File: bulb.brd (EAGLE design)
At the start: 24 x 40 mm, 9 parts, among them U1 RFD22102, U2 IC REG LDO 3.3V

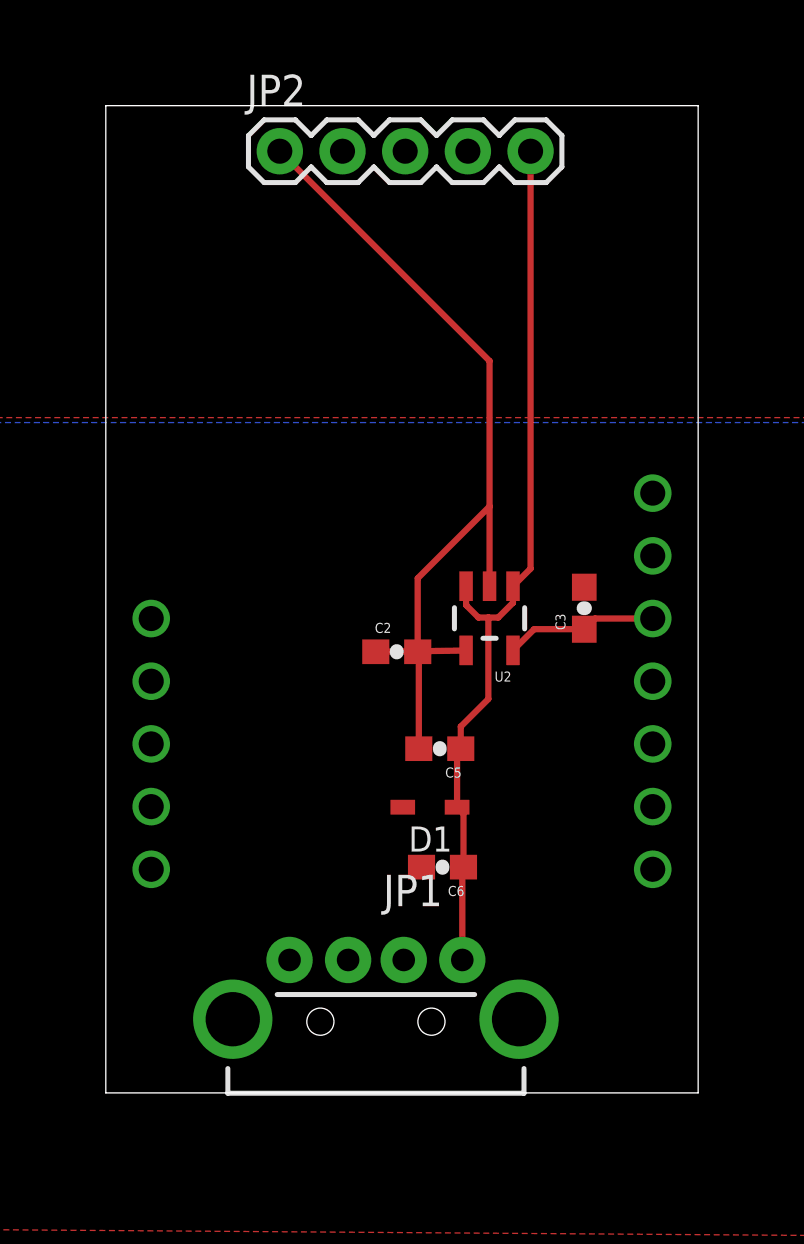
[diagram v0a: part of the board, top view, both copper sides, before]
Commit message: circle pcb, and updated usb pcb
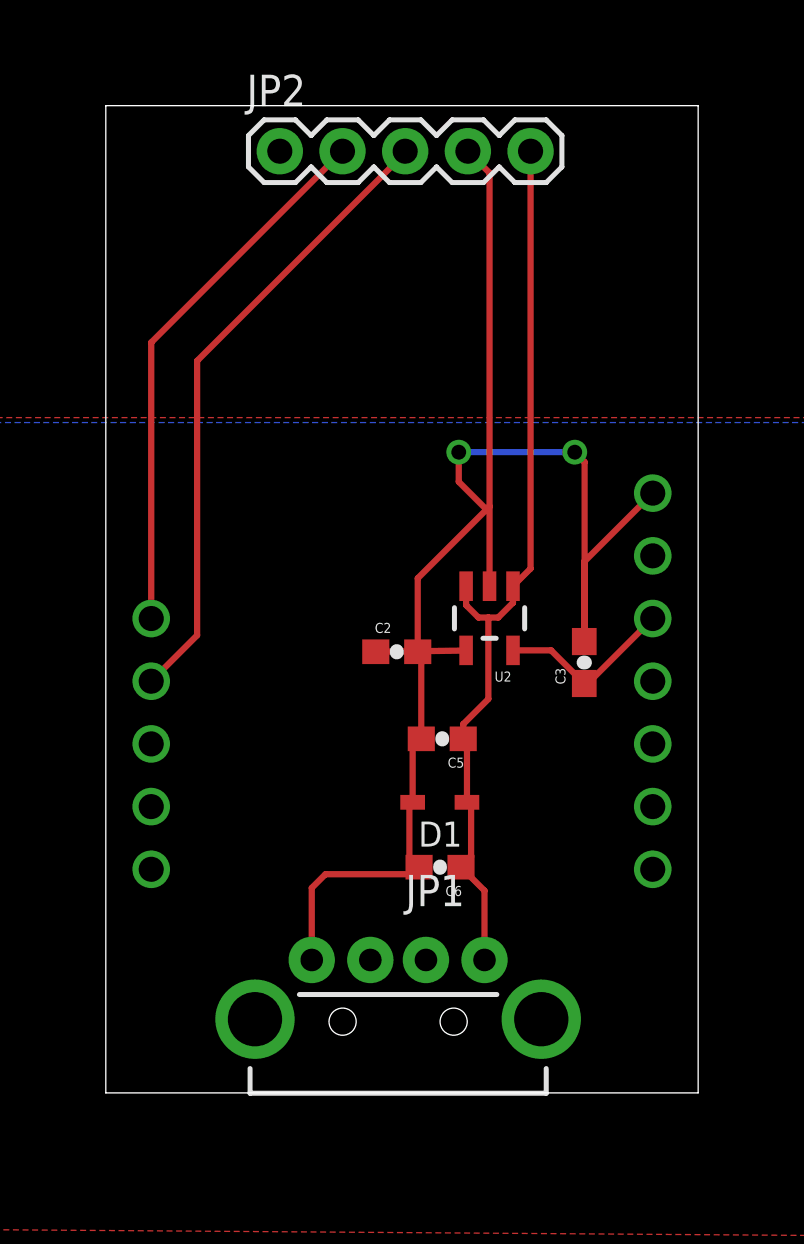
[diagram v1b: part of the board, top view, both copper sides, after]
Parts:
- moved C3 2.20 mm to (20.7, 32.0)
- moved JP1 0.90 mm to (13.1, 17.5)
- moved D1 0.45 mm to (14.8, 26.3)
- moved C5 0.41 mm to (14.9, 28.9)
- moved C6 0.10 mm to (14.8, 23.7)
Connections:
- removed net B: JP2.2
- removed net G: JP2.3
- removed net R: JP2.4
- new net DIN: JP2.3, U1.GPIO5
- new net DOUT: JP2.2, U1.GPIO6
- net GND: now also JP2.4; no longer JP2.1
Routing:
- net GND: track 32.2 -> 64.4 mm, vias 0 -> 2
- net DIN: track 0.00 -> 25.7 mm
- net DOUT: track 0.00 -> 22.1 mm
- net 3.3V: track 6.20 -> 7.31 mm
- net VBUS: track 36.2 -> 36.9 mm
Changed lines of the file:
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@@
 <attribute name="PROD_ID" value="CAP-07884" x="52.458" y="-14.576" size="1.778" layer="27" display="off"/>
 </element>
-<element name="C3" library="SparkFun-Capacitors" package="0603-CAP" value="2.2uF" x="20.686" y="34.178" rot="R90">
-<attribute name="PROD_ID" value="CAP-07888" x="67.676" y="77.358" size="1.778" layer="27" rot="R90" display="off"/>
+<element name="C3" library="SparkFun-Capacitors" package="0603-CAP" value="2.2uF" x="20.686" y="31.978" rot="R90">
+<attribute name="PROD_ID" value="CAP-07888" x="67.676" y="75.158" size="1.778" layer="27" rot="R90" display="off"/>
 </element>
-<element name="C5" library="SparkFun-Capacitors" package="0603-CAP" value="4.7uF" x="14.832" y="28.486" rot="R180">
-<attribute name="PROD_ID" value="CAP-08280" x="-32.158" y="75.476" size="1.778" layer="27" rot="R180" display="off"/>
+<element name="C5" library="SparkFun-Capacitors" package="0603-CAP" value="4.7uF" x="14.932" y="28.886" rot="R180">
+<attribute name="PROD_ID" value="CAP-08280" x="-32.058" y="75.876" size="1.778" layer="27" rot="R180" display="off"/>
 </element>
-<element name="C6" library="SparkFun-Capacitors" package="0603-CAP" value="10nF" x="14.942" y="23.686" rot="R180">
-<attribute name="PROD_ID" value="CAP-00867" x="-35.858" y="70.676" size="1.778" layer="27" rot="R180" display="off"/>
+<element name="C6" library="SparkFun-Capacitors" package="0603-CAP" value="10nF" x="14.842" y="23.686" rot="R180">
+<attribute name="PROD_ID" value="CAP-00867" x="-35.958" y="70.676" size="1.778" layer="27" rot="R180" display="off"/>
 </element>
-<element name="D1" library="zetex" package="SOD323" value="TVS Diode 5VWM 9.8VDC SOD323" x="14.432" y="26.114" rot="R180">
-<attribute name="OC_NEWARK" value="79R6078" x="-21.128" y="73.104" size="1.778" layer="27" rot="R180" display="off"/>
-<attribute name="MPN" value="CDSOD323-T05C" x="-21.128" y="73.104" size="1.778" layer="27" rot="R180" display="off"/>
-<attribute name="MF" value="" x="-21.128" y="73.104" size="1.778" layer="27" rot="R180" display="off"/>
-<attribute name="OC_FARNELL" value="1824860" x="-21.128" y="73.104" size="1.778" layer="27" rot="R180" display="off"/>
+<element name="D1" library="zetex" package="SOD323" value="TVS Diode 5VWM 9.8VDC SOD323" x="14.832" y="26.314" rot="R180">
+<attribute name="OC_NEWARK" value="79R6078" x="-20.728" y="73.304" size="1.778" layer="27" rot="R180" display="off"/>
+<attribute name="MPN" value="CDSOD323-T05C" x="-20.728" y="73.304" size="1.778" layer="27" rot="R180" display="off"/>
+<attribute name="MF" value="" x="-20.728" y="73.304" size="1.778" layer="27" rot="R180" display="off"/>
+<attribute name="OC_FARNELL" value="1824860" x="-20.728" y="73.304" size="1.778" layer="27" rot="R180" display="off"/>
 </element>
-<element name="JP1" library="SparkFun-Connectors" package="USB-A-H" value="USB-A-H" x="12.244" y="17.526" rot="R90"/>
+<element name="JP1" library="SparkFun-Connectors" package="USB-A-H" value="USB-A-H" x="13.144" y="17.526" rot="R90"/>
 <element name="JP2" library="SparkFun-Connectors" package="1X05" value="" x="8.35" y="52.694"/>
 <element name="U1" library="RF_Digital_RFD22102_Eagle_Schematic_PCB_Library" package="RFD22102" value="RFD22102" x="13.3" y="36.3" rot="MR0"/>
@@
 <contactref element="C2" pad="2"/>
 <contactref element="C3" pad="2"/>
-<contactref element="JP2" pad="1"/>
 <contactref element="JP1" pad="GND"/>
 <polygon width="0.4064" layer="1">
@@
 </polygon>
 <contactref element="U1" pad="GND"/>
+<wire x1="13.938" y1="32.414" x2="13.938" y2="35.39" width="0.254" layer="1"/>
+<wire x1="13.938" y1="35.39" x2="16.724" y2="38.176" width="0.254" layer="1"/>
+<wire x1="16.724" y1="38.176" x2="16.848" y2="38.3" width="0.254" layer="1"/>
+<wire x1="13.982" y1="32.37" x2="13.938" y2="32.414" width="0.254" layer="1"/>
+<contactref element="JP2" pad="4"/>
 <wire x1="16.848" y1="35.0701" x2="16.848" y2="38.3" width="0.254" layer="1"/>
-<wire x1="16.848" y1="38.3" x2="16.848" y2="44.196" width="0.254" layer="1"/>
-<wire x1="16.848" y1="44.196" x2="8.35" y2="52.694" width="0.254" layer="1"/>
-<wire x1="13.938" y1="32.414" x2="13.938" y2="35.39" width="0.254" layer="1"/>
-<wire x1="13.938" y1="35.39" x2="16.848" y2="38.3" width="0.254" layer="1"/>
-<wire x1="13.982" y1="28.486" x2="13.982" y2="32.37" width="0.254" layer="1"/>
-<wire x1="13.982" y1="32.37" x2="13.938" y2="32.414" width="0.254" layer="1"/>
+<wire x1="15.97" y1="52.694" x2="16.848" y2="51.816" width="0.254" layer="1"/>
+<wire x1="16.848" y1="51.816" x2="16.848" y2="38.3" width="0.254" layer="1"/>
+<wire x1="14.082" y1="28.886" x2="14.082" y2="32.27" width="0.254" layer="1"/>
+<wire x1="14.082" y1="32.27" x2="13.938" y2="32.414" width="0.254" layer="1"/>
+<wire x1="13.732" y1="26.314" x2="13.732" y2="28.536" width="0.254" layer="1"/>
+<wire x1="13.732" y1="28.536" x2="14.082" y2="28.886" width="0.254" layer="1"/>
+<wire x1="13.732" y1="26.314" x2="13.732" y2="26.232" width="0.254" layer="1"/>
+<wire x1="13.732" y1="26.232" x2="13.6" y2="26.1" width="0.254" layer="1"/>
+<wire x1="13.6" y1="26.1" x2="13.6" y2="24.078" width="0.254" layer="1"/>
+<wire x1="13.6" y1="24.078" x2="13.992" y2="23.686" width="0.254" layer="1"/>
+<wire x1="9.644" y1="19.926" x2="9.644" y2="22.844" width="0.254" layer="1"/>
+<wire x1="9.644" y1="22.844" x2="10.2" y2="23.4" width="0.254" layer="1"/>
+<wire x1="10.2" y1="23.4" x2="13.706" y2="23.4" width="0.254" layer="1"/>
+<wire x1="13.706" y1="23.4" x2="13.992" y2="23.686" width="0.254" layer="1"/>
+<wire x1="20.686" y1="32.828" x2="20.686" y2="36.066" width="0.254" layer="1"/>
+<wire x1="20.686" y1="36.066" x2="23.46" y2="38.84" width="0.254" layer="1"/>
+<wire x1="20.686" y1="32.828" x2="20.686" y2="32.886" width="0.254" layer="1"/>
+<wire x1="20.686" y1="32.886" x2="20.7" y2="32.9" width="0.254" layer="1"/>
+<wire x1="20.7" y1="32.9" x2="20.7" y2="40.1" width="0.254" layer="1"/>
+<wire x1="20.7" y1="40.1" x2="20.3" y2="40.5" width="0.254" layer="1"/>
+<via x="20.3" y="40.5" extent="1-16" drill="0.6" shape="square"/>
+<wire x1="20.3" y1="40.5" x2="15.6" y2="40.5" width="0.254" layer="16"/>
+<via x="15.6" y="40.5" extent="1-16" drill="0.6" shape="square"/>
+<wire x1="15.6" y1="40.5" x2="15.6" y2="39.3" width="0.254" layer="1"/>
+<wire x1="15.6" y1="39.3" x2="16.724" y2="38.176" width="0.254" layer="1"/>
 </signal>
 <signal name="3.3V">
@@
 <contactref element="C3" pad="1"/>
 <contactref element="U1" pad="VCC"/>
-<wire x1="17.798" y1="32.4699" x2="18.6561" y2="33.328" width="0.254" layer="1"/>
-<wire x1="18.6561" y1="33.328" x2="20.686" y2="33.328" width="0.254" layer="1"/>
-<wire x1="20.686" y1="33.328" x2="21.118" y2="33.76" width="0.254" layer="1"/>
-<wire x1="21.118" y1="33.76" x2="23.46" y2="33.76" width="0.254" layer="1"/>
+<wire x1="20.686" y1="31.128" x2="20.828" y2="31.128" width="0.254" layer="1"/>
+<wire x1="20.828" y1="31.128" x2="23.46" y2="33.76" width="0.254" layer="1"/>
+<wire x1="20.686" y1="31.128" x2="19.3441" y2="32.4699" width="0.254" layer="1"/>
+<wire x1="19.3441" y1="32.4699" x2="17.798" y2="32.4699" width="0.254" layer="1"/>
 </signal>
 <signal name="N$2">
@@
 <wire x1="17.798" y1="34.398" x2="17.798" y2="35.0701" width="0.254" layer="1"/>
 <wire x1="16.8" y1="30.5" x2="16.8" y2="33.8" width="0.254" layer="1"/>
-<wire x1="15.682" y1="28.486" x2="15.682" y2="29.382" width="0.254" layer="1"/>
-<wire x1="15.682" y1="29.382" x2="16.8" y2="30.5" width="0.254" layer="1"/>
-<wire x1="15.744" y1="19.926" x2="15.744" y2="23.638" width="0.254" layer="1"/>
-<wire x1="15.744" y1="23.638" x2="15.792" y2="23.686" width="0.254" layer="1"/>
-<wire x1="15.792" y1="23.686" x2="15.792" y2="25.854" width="0.254" layer="1"/>
-<wire x1="15.792" y1="25.854" x2="15.532" y2="26.114" width="0.254" layer="1"/>
-<wire x1="15.532" y1="26.114" x2="15.532" y2="28.336" width="0.254" layer="1"/>
-<wire x1="15.532" y1="28.336" x2="15.682" y2="28.486" width="0.254" layer="1"/>
+<wire x1="15.744" y1="23.638" x2="15.692" y2="23.686" width="0.254" layer="1"/>
+<wire x1="15.782" y1="28.886" x2="15.782" y2="29.482" width="0.254" layer="1"/>
+<wire x1="15.782" y1="29.482" x2="16.8" y2="30.5" width="0.254" layer="1"/>
+<wire x1="15.932" y1="26.314" x2="15.932" y2="28.736" width="0.254" layer="1"/>
+<wire x1="15.932" y1="28.736" x2="15.782" y2="28.886" width="0.254" layer="1"/>
+<wire x1="15.932" y1="26.314" x2="16.086" y2="26.314" width="0.254" layer="1"/>
+<wire x1="16.086" y1="26.314" x2="16.1" y2="26.3" width="0.254" layer="1"/>
+<wire x1="16.1" y1="26.3" x2="16.1" y2="24.094" width="0.254" layer="1"/>
+<wire x1="16.1" y1="24.094" x2="15.692" y2="23.686" width="0.254" layer="1"/>
+<wire x1="16.644" y1="19.926" x2="16.644" y2="22.734" width="0.254" layer="1"/>
+<wire x1="16.644" y1="22.734" x2="15.692" y2="23.686" width="0.254" layer="1"/>
 </signal>
-<signal name="R">
-<contactref element="JP2" pad="4"/>
+<signal name="DIN">
+<contactref element="U1" pad="GPIO5"/>
+<contactref element="JP2" pad="3"/>
+<wire x1="3.14" y1="31.22" x2="5" y2="33.08" width="0.254" layer="1"/>
+<wire x1="5" y1="33.08" x2="5" y2="44.2" width="0.254" layer="1"/>
+<wire x1="5" y1="44.2" x2="13.43" y2="52.63" width="0.254" layer="1"/>
+<wire x1="13.43" y1="52.63" x2="13.43" y2="52.694" width="0.254" layer="1"/>
 </signal>
-<signal name="G">
-<contactref element="JP2" pad="3"/>
-</signal>
-<signal name="B">
+<signal name="DOUT">
+<contactref element="U1" pad="GPIO6"/>
 <contactref element="JP2" pad="2"/>
+<wire x1="3.14" y1="33.76" x2="3.14" y2="44.944" width="0.254" layer="1"/>
+<wire x1="3.14" y1="44.944" x2="10.89" y2="52.694" width="0.254" layer="1"/>
 </signal>
 </signals>

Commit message: updated pcbs
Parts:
- added R1: 470, resistor:R0603
- moved JP2 4.51 mm to (8.10, 57.2)
- moved C2 0.53 mm to (12.6, 32.6), turned to 180 degrees
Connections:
- removed net DIN: JP2.3, U1.GPIO5
- new net DIN-H: JP2.3, R1.1
- new net DIN-RF: R1.2, U1.GPIO5
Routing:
- net DIN: track 25.7 -> 0.00 mm
- net DIN-H: track 0.00 -> 19.4 mm
- net DIN-RF: track 0.00 -> 9.09 mm
- net GND: track 64.4 -> 70.4 mm
- net VBUS: track 36.9 -> 41.7 mm
- net DOUT: track 22.1 -> 26.6 mm
- net N$2: track 3.66 -> 2.51 mm
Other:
- board size 24 x 40 mm -> 24 x 45 mm
